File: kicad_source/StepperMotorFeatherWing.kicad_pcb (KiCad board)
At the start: 2 copper layers, 100 x 60 mm, 102 parts, among them CN1 ADAFRUIT_FEATHER, P1 WR-TBL_691322310002, P10 CONN_01X04, P2 WR-TBL_691313710002, P3 CONN_01X04, P4 CONN_01X05, P5 CONN_01X04, P6 CONN_01X05, P7 CONN_01X04, P8 CONN_01X04, P9 CONN_01X04, Q1 IPD90P03P4L- 04, U1 TMC5130A-TA, U2 TMC5130A-TA, U3 LT1085, U9 IFX91041EJV, Y1 oscillator

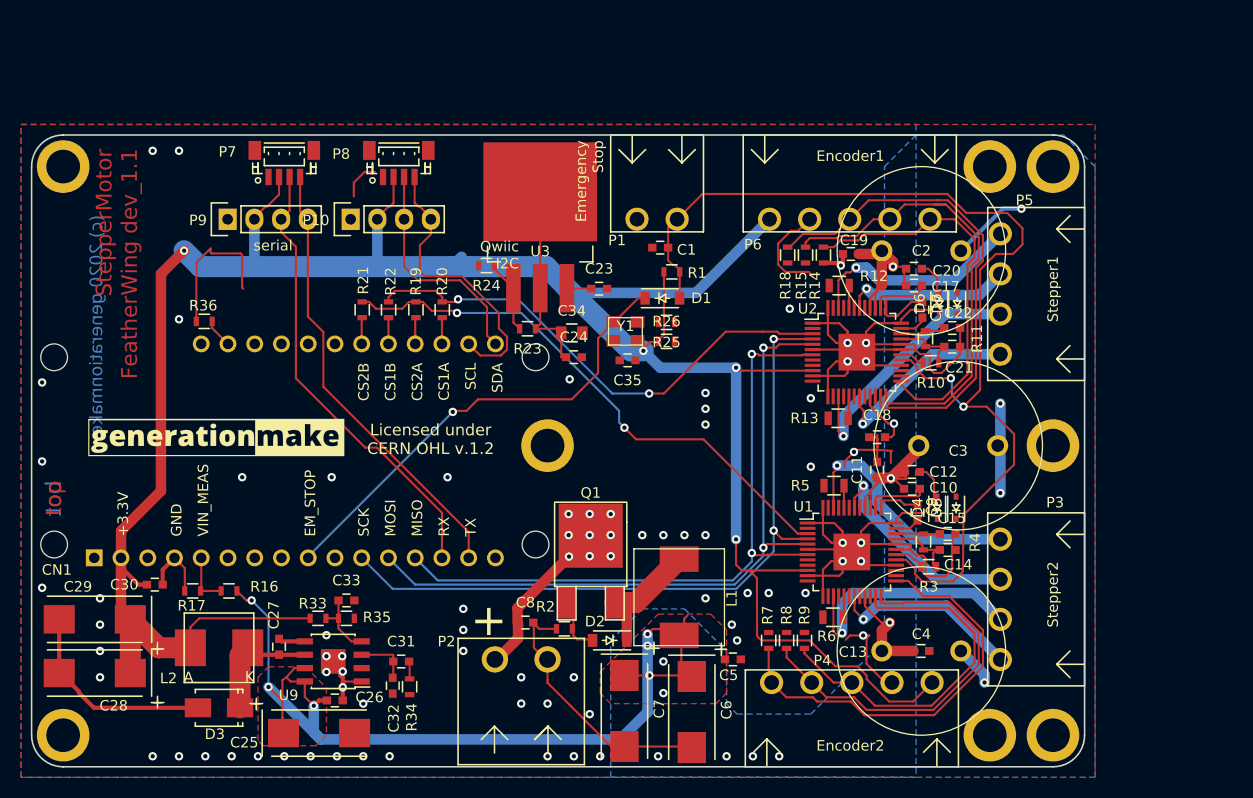
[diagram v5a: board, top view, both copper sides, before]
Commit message: added leds and decoupling capacitors
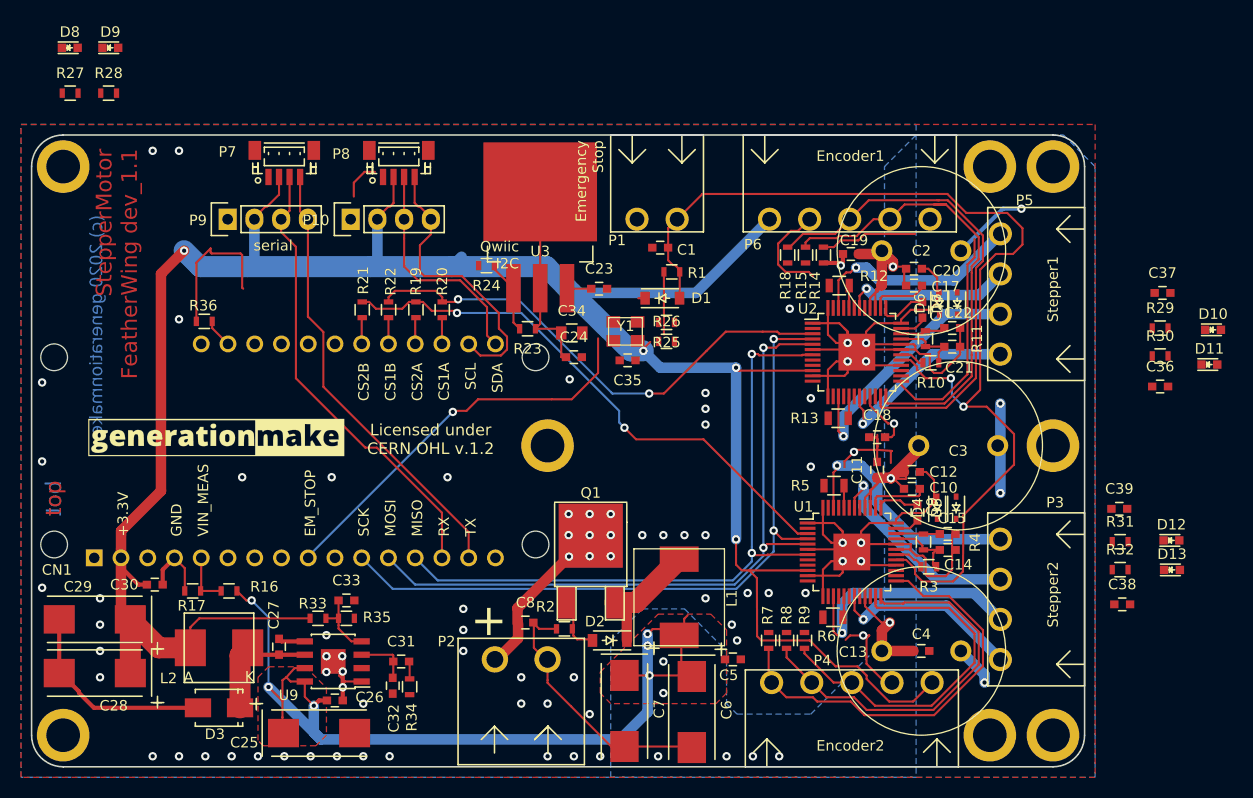
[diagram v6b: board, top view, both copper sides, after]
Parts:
- added C36: 100nF, capacitors:C_0603, F.Cu at (158.2, 89.9)
- added C37: 100nF, capacitors:C_0603, F.Cu at (158.4, 81.0)
- added C38: 100nF, capacitors:C_0603, F.Cu at (154.6, 110.6)
- added C39: 100nF, capacitors:C_0603, F.Cu at (154.3, 101.5)
- added D10: Led_Small, LEDs:LED_0603, F.Cu at (163.2, 84.5)
- added D11: Led_Small, LEDs:LED_0603, F.Cu at (162.9, 87.8)
- added D12: Led_Small, LEDs:LED_0603, F.Cu at (159.2, 104.5)
- added D13: Led_Small, LEDs:LED_0603, F.Cu at (159.3, 107.3)
- added D8: Led_Small, LEDs:LED_0603, F.Cu at (54.6, 57.7)
- added D9: Led_Small, LEDs:LED_0603, F.Cu at (58.5, 57.7)
- added R27: 2k2, resistors:R_0603, F.Cu at (54.7, 62.0)
- added R28: 2k2, resistors:R_0603, F.Cu at (58.3, 62.0)
- added R29: 2k2, resistors:R_0603, F.Cu at (158.2, 84.3)
- added R30: 2k2, resistors:R_0603, F.Cu at (158.2, 87.0)
- added R31: 2k2, resistors:R_0603, F.Cu at (154.4, 104.6)
- added R32: 2k2, resistors:R_0603, F.Cu at (154.4, 107.3)
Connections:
- net Net-(R12-Pad2) renamed /MotorDriver1/BRA
- net Net-(R13-Pad2) renamed /MotorDriver1/BRB
- net Net-(R5-Pad2) renamed /MotorDriver2/BRA
- net Net-(R6-Pad2) renamed /MotorDriver2/BRB
- U1 pad 26: (no net) -> /MotorDriver2/DIAG0
- U1 pad 27: (no net) -> /MotorDriver2/DIAG1
- U2 pad 26: (no net) -> /MotorDriver1/DIAG0
- U2 pad 27: (no net) -> /MotorDriver1/DIAG1
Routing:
- net /MotorDriver1/ENCA: track 38.5 -> 31.5 mm
- net EM_STOP_D: track 44.2 -> 38.8 mm
- net +3V3: track 234.3 -> 232.6 mm

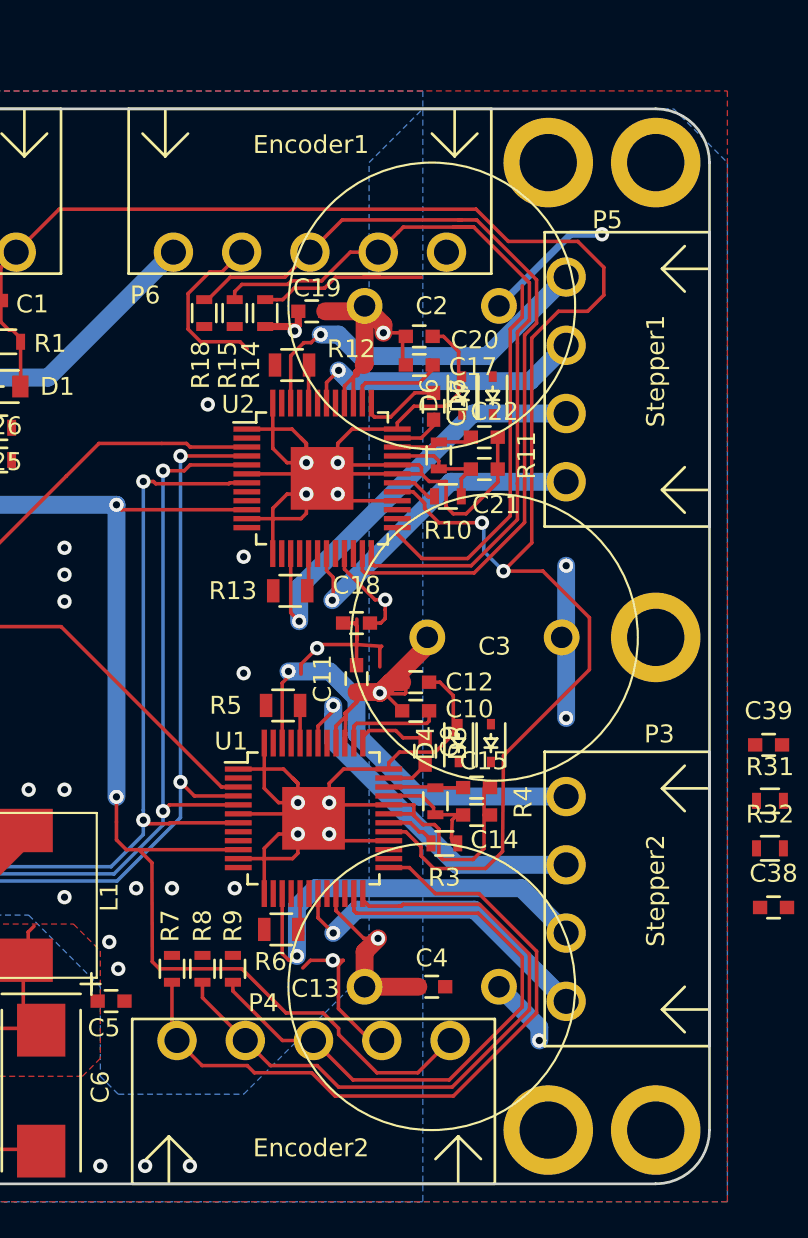
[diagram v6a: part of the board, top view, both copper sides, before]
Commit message: changed type of encoder connector
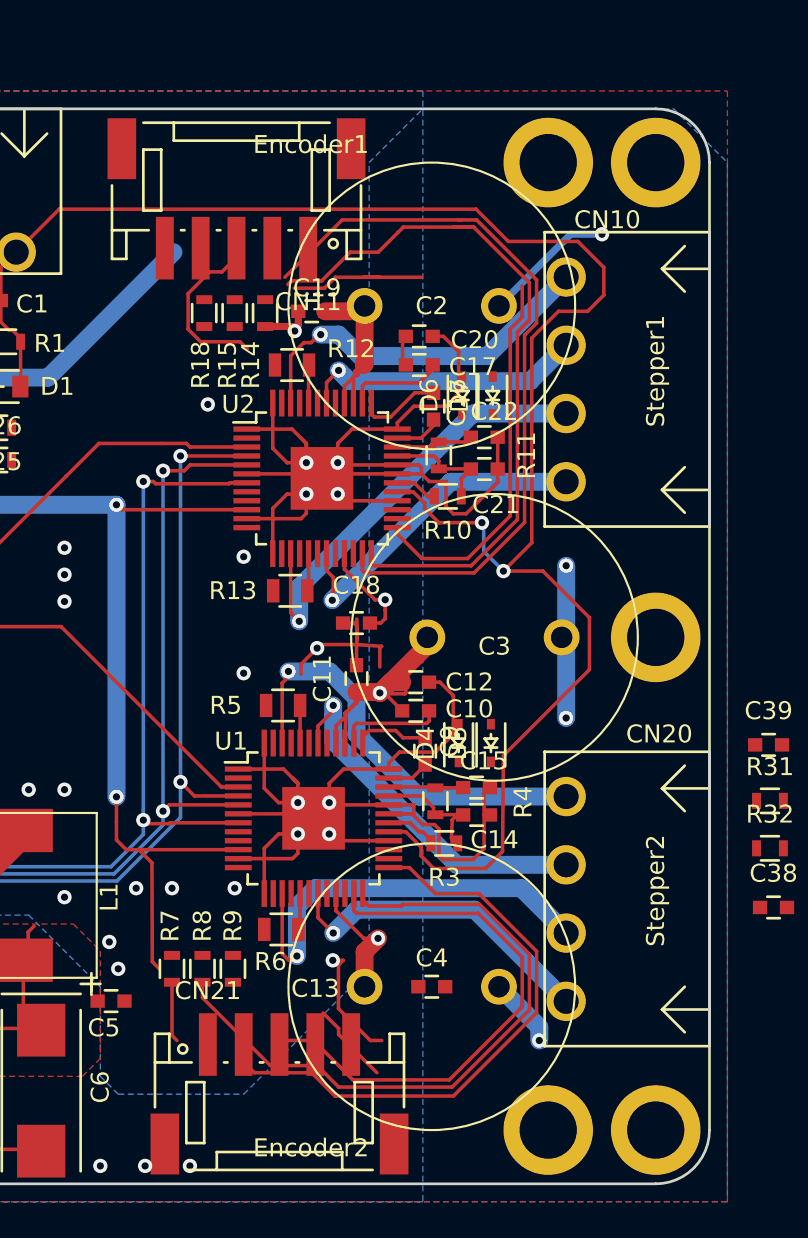
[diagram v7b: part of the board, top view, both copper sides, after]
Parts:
- removed P4, P6: CONN_01X05, CON_wuerth:WR-TBL_691322310005
- added CN11: CONN_01X05, connectors_JST_PH:Connectors_JST_S5B-PH-SM4-TB, F.Cu at (124.6, 71.0)
- added CN21: CONN_01X05, connectors_JST_PH:Connectors_JST_S5B-PH-SM4-TB, F.Cu at (127.0, 121.0)
- renumbered P5 to CN10, P3 to CN20
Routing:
- net +3V3: track 232.6 -> 217.6 mm
- net GND: track 246.8 -> 235.2 mm
- net VIN: track 145.9 -> 139.9 mm, vias 12 -> 11
- net /MotorDriver1/ENCN: track 46.8 -> 51.7 mm
- net /MotorDriver2/ENCA: track 40.3 -> 35.8 mm
- net /MotorDriver2/ENCN: track 34.6 -> 30.2 mm
- net /MotorDriver1/ENCB: track 44.2 -> 40.7 mm
- net /MotorDriver1/ENCA: track 31.5 -> 29.6 mm

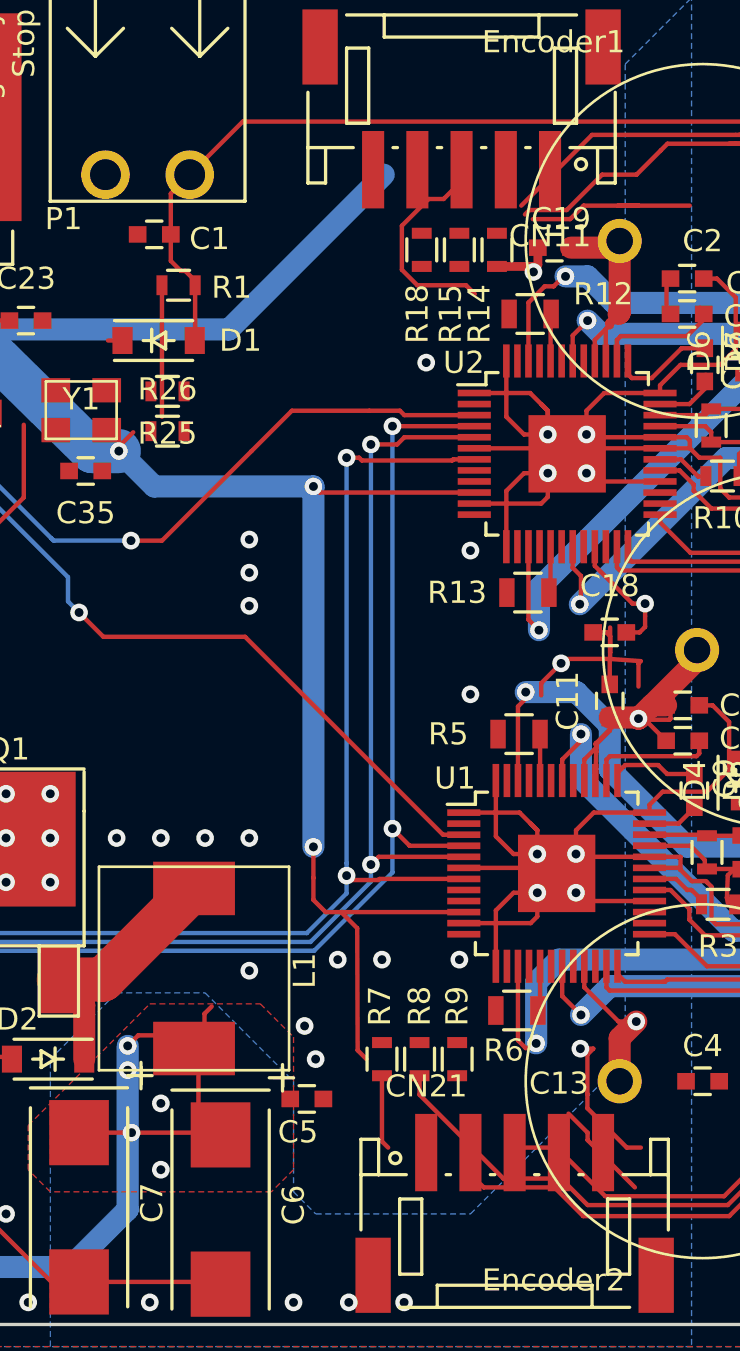
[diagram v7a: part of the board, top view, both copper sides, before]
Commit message: added temperature sensor LM75
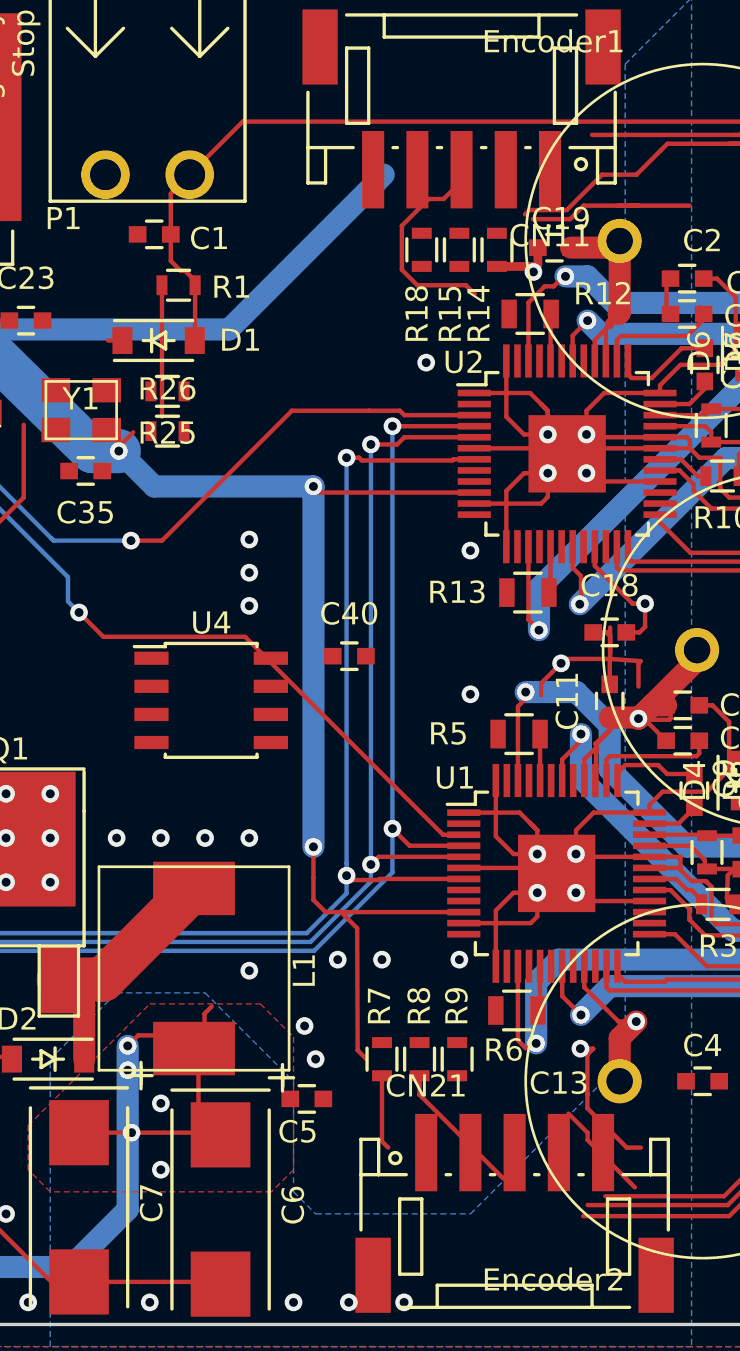
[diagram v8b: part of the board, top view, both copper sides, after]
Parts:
- added C40: 100nF, capacitors:C_0603, F.Cu at (119.5, 95.8)
- added U4: LM75, SOIC:SOIC-8_3.9x4.9mm_Pitch1.27mm, F.Cu at (113.3, 97.8)
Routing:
- net /MotorDriver2/ENCA: track 35.8 -> 30.2 mm
- net /MotorDriver2/ENCN: track 30.2 -> 25.3 mm
- net /MotorDriver1/ENCN: track 51.7 -> 47.2 mm
- net /MotorDriver2/ENCB: track 37.1 -> 32.8 mm
